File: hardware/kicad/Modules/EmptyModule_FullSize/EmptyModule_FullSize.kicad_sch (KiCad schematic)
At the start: 2 parts, among them J1 Conn_02x04_Odd_Even, J2 Conn_02x04_Odd_Even

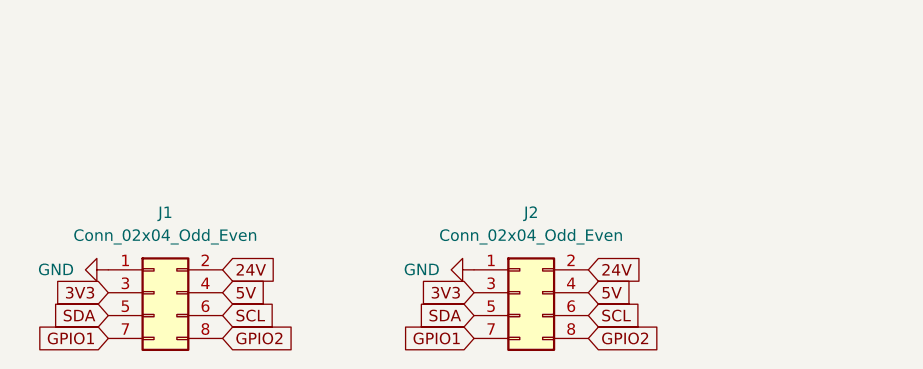
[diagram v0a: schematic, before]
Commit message: feat(hardware): update FullSize empty module template
- update schematic and PCB from the daughterboard design block
- preserve linked design block groups and connector references
- correct connector alignment and power routing widths
- remove duplicate same-net routing
- validate pinout, geometry, ERC, and DRC
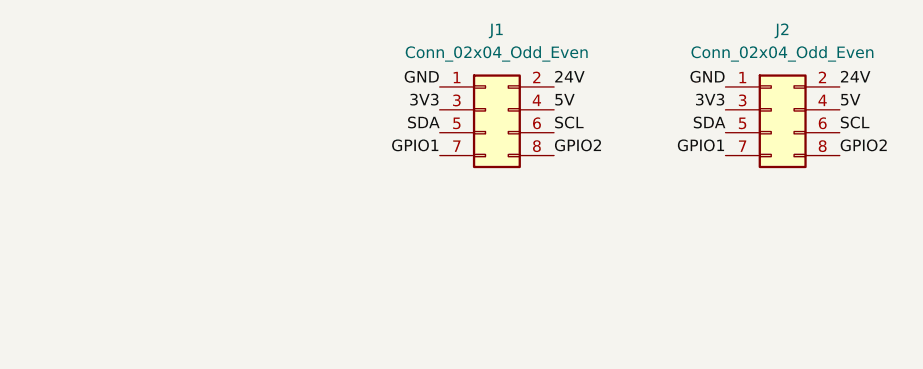
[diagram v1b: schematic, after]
